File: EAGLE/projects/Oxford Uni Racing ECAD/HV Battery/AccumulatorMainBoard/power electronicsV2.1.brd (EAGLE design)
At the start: 160 x 100 mm, 100 parts, among them IC1 4043D, IC10 74AHC1G08DBV, IC2 SE555D, IC3 4011D, IC5 4043D, IC6 4011D, IC7 4011D, IC8 4011D, IC9 4011D, K1 T9AS1D12-48=T9A, K2 T9AS5D12-12=T9A, K3 T9AS1D12-48=T9A, K4 T9AS1D12-48=T9A, Q1 BSS138, Q2 BSS138, Q3 BSS138, Q4 BSS138

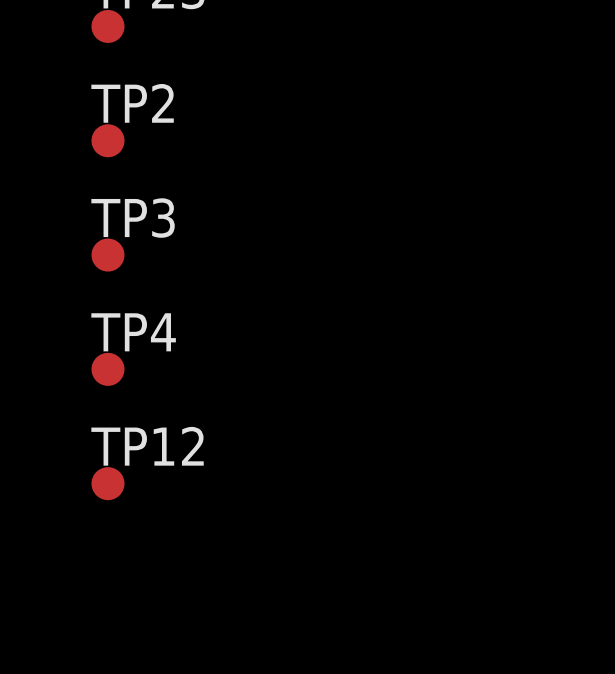
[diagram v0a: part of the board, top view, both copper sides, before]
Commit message: small changes to schematic on acc main board and more feedback
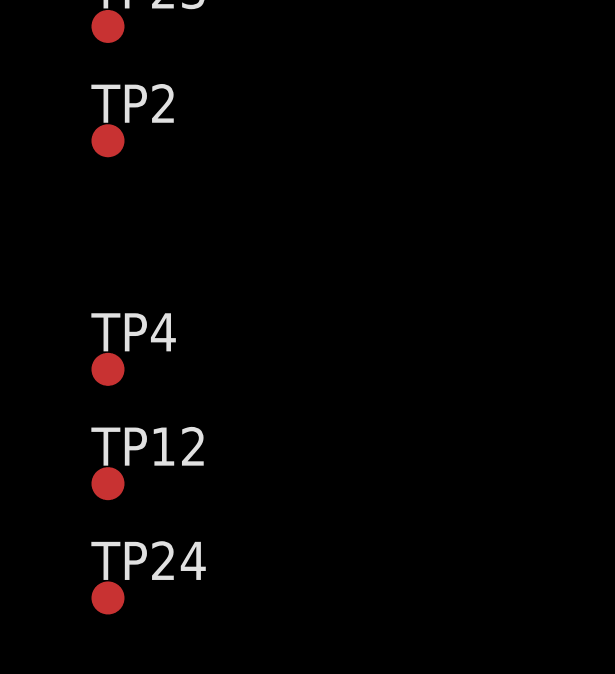
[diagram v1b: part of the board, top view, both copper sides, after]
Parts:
- removed TP3: TPSTP11R, testpad:TP11R
- added TP24: TPSTP11R, testpad:TP11R
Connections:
- net +12V: no longer C9.2, IC1.11, IC1.12, IC1.14, IC1.15, K1.3, K4.4, OK2.5, PRECHARGE/AIRS.3, PRECHARGE/AIRS.4, PRECHARGE/AIRS.6, Q1.2, Q2.2, Q4.2, R13.1, R19.1, R3.2, TP11.TP, TP14.TP, TP3.TP
- net GND: now also C9.2, IC1.11, IC1.12, IC1.14, IC1.15, K1.3, K4.4, OK2.5, PRECHARGE/AIRS.3, PRECHARGE/AIRS.4, PRECHARGE/AIRS.6, Q1.2, Q2.2, Q4.2, R13.1, R19.1, R3.2, TP11.TP, TP14.TP, TP24.TP

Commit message: most of the feedback addressed
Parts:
- removed IC10: 74AHC1G08DBV, 74xx-little-us:SOT23-5
- added LED7, LED8: (no value), led:SML0805
- added R12, R14, R15: (no value), rcl:R0805
- TP1, TP10, TP11, TP12, TP13, TP14, TP15, TP16, TP17, TP18, TP19, TP2, TP20, TP21, TP22, TP23, TP24, TP4, TP5, TP6, TP7: value TPSTP11R -> TPPAD1-17; device testpad:TP11R -> testpad:P1-17
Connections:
- removed net VCC: IC10.5
- new net N$18: LED7.A, R14.1
- new net N$20: LED8.A, R15.1
- new net N$6: IC9.11, IC9.8, IC9.9
- net +12V: now also R14.2, R15.2; no longer IC10.3
- net CHARGE_SAFE: now also IC9.12; no longer IC10.1
- net DISCHARGE_ENABLE: now also R12.2
- net GND: now also R12.1; no longer IC9.12, IC9.13, IC9.8, IC9.9
- net IMD_COIL_OUT: now also LED8.C
- net N$1: now also IC9.10; no longer IC10.4
- net N$13: now also IC9.13; no longer IC10.2
- net N$15: now also LED7.C

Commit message: most of the feedback addressed ctd
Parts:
- removed R17: (no value), rcl:R0805
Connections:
- removed net N$13: IC9.13, LED4.C
- net DISCHARGE_ENABLE: now also IC9.13, LED4.C
- net GND: no longer R17.1
- net N$8: no longer R17.2
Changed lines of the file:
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@@
 <attribute name="VALUE" x="-36.195" y="143.51" size="1.27" layer="27"/>
-</element>
-<element name="R17" library="rcl" library_urn="urn:adsk.eagle:library:334" package="R0805" package3d_urn="urn:adsk.eagle:package:23553/2" value="" x="-41.91" y="146.05" smashed="yes">
-<attribute name="NAME" x="-42.545" y="147.32" size="1.27" layer="25"/>
-<attribute name="POPULARITY" value="86" x="0" y="0" size="1.778" layer="27" display="off"/>
-<attribute name="SPICEPREFIX" value="R" x="0" y="0" size="1.778" layer="27" display="off"/>
-<attribute name="VALUE" x="-42.545" y="143.51" size="1.27" layer="27"/>
 </element>
 <element name="R19" library="rcl" library_urn="urn:adsk.eagle:library:334" package="R0805" package3d_urn="urn:adsk.eagle:package:23553/2" value="" x="-48.26" y="146.05" smashed="yes">
@@
 <contactref element="C1" pad="2"/>
 <contactref element="C2" pad="2"/>
-<contactref element="R17" pad="1"/>
 <contactref element="IC4" pad="3"/>
 <contactref element="C4" pad="2"/>
@@
 <wire x1="-55.56" y1="146.05" x2="-58.74" y2="140.97" width="0" layer="19" extent="1-1"/>
 <wire x1="-49.21" y1="146.05" x2="-55.56" y2="146.05" width="0" layer="19" extent="1-1"/>
-<wire x1="-42.86" y1="146.05" x2="-49.21" y2="146.05" width="0" layer="19" extent="1-1"/>
-<wire x1="-44.72" y1="151.13" x2="-42.86" y2="146.05" width="0" layer="19" extent="1-1"/>
-<wire x1="-36.51" y1="146.05" x2="-42.86" y2="146.05" width="0" layer="19" extent="1-1"/>
+<wire x1="-44.72" y1="151.13" x2="-49.21" y2="146.05" width="0" layer="19" extent="1-1"/>
+<wire x1="-36.51" y1="146.05" x2="-44.72" y2="151.13" width="0" layer="19" extent="1-1"/>
 <wire x1="-28.89" y1="140.97" x2="-36.51" y2="146.05" width="0" layer="19" extent="1-1"/>
 <wire x1="-15.56" y1="140.97" x2="-28.89" y2="140.97" width="0" layer="19" extent="1-1"/>
@@
 <contactref element="TP18" pad="TP"/>
 <contactref element="R12" pad="2"/>
+<contactref element="LED4" pad="C"/>
+<contactref element="IC9" pad="13"/>
 <wire x1="-124.78" y1="-133.35" x2="-125.73" y2="-82.55" width="0" layer="19" extent="1-1"/>
 <wire x1="-118.11" y1="-16.51" x2="-125.73" y2="-82.55" width="0" layer="19" extent="1-1"/>
-<wire x1="-67.31" y1="113.7666" x2="-118.11" y2="-16.51" width="0" layer="19" extent="1-1"/>
+<wire x1="-116.84" y1="119.9134" x2="-118.11" y2="-16.51" width="0" layer="19" extent="1-1"/>
+<wire x1="-92.39" y1="124.53" x2="-116.84" y2="119.9134" width="0" layer="19" extent="1-1"/>
+<wire x1="-92.49" y1="146.05" x2="-92.39" y2="124.53" width="0" layer="19" extent="1-1"/>
+<wire x1="-67.31" y1="113.7666" x2="-92.39" y2="124.53" width="0" layer="19" extent="1-1"/>
 <wire x1="-66.04" y1="113.7666" x2="-67.31" y2="113.7666" width="0" layer="19" extent="1-1"/>
-<wire x1="-92.39" y1="124.53" x2="-67.31" y2="113.7666" width="0" layer="19" extent="1-1"/>
 <wire x1="-38.735" y1="119.9134" x2="-66.04" y2="113.7666" width="0" layer="19" extent="1-1"/>
 <wire x1="-31.75" y1="151.13" x2="-38.735" y2="119.9134" width="0" layer="19" extent="1-1"/>
@@
 </signal>
 <signal name="CHARGE_SAFE">
-<contactref element="LED5" pad="C"/>
 <contactref element="BMS_I/O" pad="2"/>
 <contactref element="IC9" pad="12"/>
+<contactref element="LED5" pad="C"/>
 <wire x1="-115.57" y1="119.9134" x2="-120.65" y2="-16.51" width="0" layer="19" extent="1-1"/>
 <wire x1="-98.84" y1="146.05" x2="-115.57" y2="119.9134" width="0" layer="19" extent="1-1"/>
@@
 <wire x1="-46.72" y1="151.13" x2="-41.275" y2="113.7666" width="0" layer="19" extent="1-1"/>
 <wire x1="-65.09" y1="146.05" x2="-46.72" y2="151.13" width="0" layer="19" extent="1-1"/>
-</signal>
-<signal name="N$13">
-<contactref element="LED4" pad="C"/>
-<contactref element="IC9" pad="13"/>
-<wire x1="-116.84" y1="119.9134" x2="-92.49" y2="146.05" width="0" layer="19" extent="1-1"/>
 </signal>
 <signal name="N$9">
@@
 <contactref element="Q2" pad="1"/>
 <contactref element="TP6" pad="TP"/>
-<contactref element="R17" pad="2"/>
 <contactref element="R24" pad="2"/>
 <contactref element="TP17" pad="TP"/>
@@
 <wire x1="-100.01" y1="124.53" x2="-80.01" y2="119.9134" width="0" layer="19" extent="1-1"/>
 <wire x1="-53.66" y1="146.05" x2="-80.01" y2="119.9134" width="0" layer="19" extent="1-1"/>
-<wire x1="-40.96" y1="146.05" x2="-53.66" y2="146.05" width="0" layer="19" extent="1-1"/>
-<wire x1="-26.67" y1="151.13" x2="-40.96" y2="146.05" width="0" layer="19" extent="1-1"/>
+<wire x1="-26.67" y1="151.13" x2="-53.66" y2="146.05" width="0" layer="19" extent="1-1"/>
 </signal>
 <signal name="N$14">

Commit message: Minor changes to layout added values to RC circuit
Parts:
- C9: value (none) -> DNP
- R2: value (none) -> 0R
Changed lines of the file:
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@@
 <attribute name="VALUE" x="-17.78" y="138.43" size="1.27" layer="27"/>
 </element>
-<element name="C9" library="rcl" library_urn="urn:adsk.eagle:library:334" package="C0805K" package3d_urn="urn:adsk.eagle:package:23681/2" value="" x="-45.72" y="151.13" smashed="yes">
+<element name="C9" library="rcl" library_urn="urn:adsk.eagle:library:334" package="C0805K" package3d_urn="urn:adsk.eagle:package:23681/2" value="DNP" x="-45.72" y="151.13" smashed="yes">
 <attribute name="NAME" x="-46.72" y="152.005" size="1.016" layer="25"/>
 <attribute name="POPULARITY" value="52" x="0" y="0" size="1.778" layer="27" display="off"/>
@@
 <attribute name="VALUE" x="-48.895" y="143.51" size="1.27" layer="27"/>
 </element>
-<element name="R2" library="rcl" library_urn="urn:adsk.eagle:library:334" package="R0805" package3d_urn="urn:adsk.eagle:package:23553/2" value="" x="-66.04" y="146.05" smashed="yes">
+<element name="R2" library="rcl" library_urn="urn:adsk.eagle:library:334" package="R0805" package3d_urn="urn:adsk.eagle:package:23553/2" value="0R" x="-66.04" y="146.05" smashed="yes">
 <attribute name="NAME" x="-66.675" y="147.32" size="1.27" layer="25"/>
 <attribute name="POPULARITY" value="86" x="0" y="0" size="1.778" layer="27" display="off"/>
@@
 <contactref element="IC1" pad="14"/>
 <contactref element="IC1" pad="15"/>
-<contactref element="Q1" pad="2"/>
 <contactref element="R3" pad="2"/>
 <contactref element="OK2" pad="5"/>
@@
 <contactref element="TP14" pad="TP"/>
 <contactref element="TP24" pad="TP"/>
+<contactref element="Q1" pad="2"/>
 <contactref element="R12" pad="1"/>
 <wire x1="-126.68" y1="-133.35" x2="-125.73" y2="-128.27" width="0" layer="19" extent="1-1"/>
@@
 </signal>
 <signal name="DISCHARGE_ENABLE">
-<contactref element="IC3" pad="5"/>
-<contactref element="IC3" pad="6"/>
 <contactref element="Q1" pad="1"/>
 <contactref element="TP7" pad="TP"/>
@@
 <contactref element="LED4" pad="C"/>
 <contactref element="IC9" pad="13"/>
+<contactref element="IC3" pad="5"/>
+<contactref element="IC3" pad="6"/>
 <wire x1="-124.78" y1="-133.35" x2="-125.73" y2="-82.55" width="0" layer="19" extent="1-1"/>
 <wire x1="-118.11" y1="-16.51" x2="-125.73" y2="-82.55" width="0" layer="19" extent="1-1"/>

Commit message: Removed some testpoints and added a few. Also fixed EMSDC relay path
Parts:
- removed R13: (no value), rcl:R0805
- removed TP14, TP15, TP18, TP22: TPPAD1-17, testpad:P1-17
- added TP3: TPPAD1-17, testpad:P1-17
- moved TP6 335.0 mm to (-125.7, -168.9)
- moved TP11 106.7 mm to (-125.7, -174.0)
- moved TP2 45.7 mm to (-125.7, -158.8)
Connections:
- new net N$13: EMSDC.1, K4.3
- new net N$21: K1.3, K4.4
- net +12V: no longer EMSDC.1, K4.3, TP15.TP, TP22.TP
- net CHARGE_SAFE: now also TP3.TP
- net DISCHARGE_ENABLE: now also TP6.TP; no longer TP18.TP
- net GND: no longer K1.3, K4.4, R13.1, TP11.TP, TP14.TP
- net N$10: no longer TP2.TP
- net N$16: now also TP2.TP
- net N$6: now also TP11.TP
- net N$8: no longer TP6.TP
- net N$9: no longer R13.2

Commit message: Updates to the accumulator main board
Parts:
- removed TP13, TP19, TP20: TPPAD1-17, testpad:P1-17
- added TP14: TPPAD1-17, testpad:P1-17
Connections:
- net GND: now also Q3.2
- net IMD_COIL_OUT: now also TP14.TP; no longer Q3.2, TP19.TP
- net N$14: no longer TP13.TP
- net N$9: no longer TP20.TP
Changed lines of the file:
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@@
 <attribute name="VALUE" x="-110.09" y="-57.3" size="1.27" layer="27" align="center"/>
-</element>
-<element name="TP19" library="testpad" library_urn="urn:adsk.eagle:library:385" package="P1-17" package3d_urn="urn:adsk.eagle:package:27949/1" value="TPPAD1-17" x="-125.73" y="-71.12" smashed="yes">
-<attribute name="NAME" x="-126.2799" y="-70.5201" size="1.27" layer="25"/>
-<attribute name="POPULARITY" value="0" x="-125.73" y="-71.12" size="1.778" layer="27" display="off"/>
-<attribute name="TP_SIGNAL_NAME" value="" x="-125.73" y="-73.025" size="1" layer="37"/>
-<attribute name="VALUE" x="-126.238" y="-71.628" size="0.0254" layer="27"/>
 </element>
 <element name="TP17" library="testpad" library_urn="urn:adsk.eagle:library:385" package="P1-17" package3d_urn="urn:adsk.eagle:package:27949/1" value="TPPAD1-17" x="-125.73" y="-74.93" smashed="yes">
@@
 <attribute name="VALUE" x="-126.238" y="-75.438" size="0.0254" layer="27"/>
 </element>
-<element name="TP20" library="testpad" library_urn="urn:adsk.eagle:library:385" package="P1-17" package3d_urn="urn:adsk.eagle:package:27949/1" value="TPPAD1-17" x="-125.73" y="-78.74" smashed="yes">
-<attribute name="NAME" x="-126.2799" y="-78.1401" size="1.27" layer="25"/>
-<attribute name="POPULARITY" value="0" x="-125.73" y="-78.74" size="1.778" layer="27" display="off"/>
-<attribute name="TP_SIGNAL_NAME" value="" x="-125.73" y="-80.645" size="1" layer="37"/>
-<attribute name="VALUE" x="-126.238" y="-79.248" size="0.0254" layer="27"/>
-</element>
 <element name="TP16" library="testpad" library_urn="urn:adsk.eagle:library:385" package="P1-17" package3d_urn="urn:adsk.eagle:package:27949/1" value="TPPAD1-17" x="-125.73" y="-86.36" smashed="yes">
 <attribute name="NAME" x="-126.2799" y="-85.7601" size="1.27" layer="25"/>
@@
 <attribute name="VALUE" x="-126.238" y="-90.678" size="0.0254" layer="27"/>
 </element>
-<element name="TP13" library="testpad" library_urn="urn:adsk.eagle:library:385" package="P1-17" package3d_urn="urn:adsk.eagle:package:27949/1" value="TPPAD1-17" x="-125.73" y="-101.6" smashed="yes">
-<attribute name="NAME" x="-126.2799" y="-101.0001" size="1.27" layer="25"/>
-<attribute name="POPULARITY" value="0" x="-125.73" y="-101.6" size="1.778" layer="27" display="off"/>
-<attribute name="TP_SIGNAL_NAME" value="" x="-125.73" y="-103.505" size="1" layer="37"/>
-<attribute name="VALUE" x="-126.238" y="-102.108" size="0.0254" layer="27"/>
-</element>
 <element name="TP23" library="testpad" library_urn="urn:adsk.eagle:library:385" package="P1-17" package3d_urn="urn:adsk.eagle:package:27949/1" value="TPPAD1-17" x="-125.73" y="-109.22" smashed="yes">
 <attribute name="NAME" x="-126.2799" y="-108.6201" size="1.27" layer="25"/>
@@
 <attribute name="TP_SIGNAL_NAME" value="" x="-125.73" y="-173.99" size="1.778" layer="27" display="off"/>
 <attribute name="VALUE" x="-125.73" y="-173.99" size="0.0254" layer="27"/>
+</element>
+<element name="TP14" library="testpad" library_urn="urn:adsk.eagle:library:385" package="P1-17" package3d_urn="urn:adsk.eagle:package:27949/1" value="TPPAD1-17" x="-125.73" y="-179.07" smashed="yes">
+<attribute name="NAME" x="-126.873" y="-177.673" size="1.27" layer="25" ratio="10"/>
+<attribute name="POPULARITY" value="0" x="-125.73" y="-179.07" size="1.778" layer="27" display="off"/>
+<attribute name="TP_SIGNAL_NAME" value="" x="-127" y="-182.245" size="1" layer="37"/>
+<attribute name="VALUE" x="-125.73" y="-179.07" size="0.0254" layer="27"/>
 </element>
 </elements>
@@
 <contactref element="IC1" pad="12"/>
 <contactref element="C9" pad="2"/>
-<contactref element="Q2" pad="2"/>
 <contactref element="TP24" pad="TP"/>
 <contactref element="Q1" pad="2"/>
 <contactref element="R12" pad="1"/>
+<contactref element="Q3" pad="2"/>
+<contactref element="Q2" pad="2"/>
 <wire x1="-126.68" y1="-133.35" x2="-125.73" y2="-128.27" width="0" layer="19" extent="1-1"/>
 <wire x1="-120.65" y1="-7.62" x2="-125.73" y2="-128.27" width="0" layer="19" extent="1-1"/>
@@
 <wire x1="-98.11" y1="124.53" x2="-99.06" y2="113.7666" width="0" layer="19" extent="1-1"/>
 <wire x1="-90.49" y1="124.53" x2="-98.11" y2="124.53" width="0" layer="19" extent="1-1"/>
-<wire x1="-99.38" y1="133.35" x2="-98.11" y2="124.53" width="0" layer="19" extent="1-1"/>
-<wire x1="-105.28" y1="133.35" x2="-99.38" y2="133.35" width="0" layer="19" extent="1-1"/>
+<wire x1="-105.73" y1="124.53" x2="-98.11" y2="124.53" width="0" layer="19" extent="1-1"/>
+<wire x1="-113.35" y1="124.53" x2="-105.73" y2="124.53" width="0" layer="19" extent="1-1"/>
+<wire x1="-105.28" y1="133.35" x2="-105.73" y2="124.53" width="0" layer="19" extent="1-1"/>
+<wire x1="-99.38" y1="133.35" x2="-105.28" y2="133.35" width="0" layer="19" extent="1-1"/>
 <wire x1="-93.03" y1="133.35" x2="-99.38" y2="133.35" width="0" layer="19" extent="1-1"/>
 <wire x1="-86.68" y1="133.35" x2="-93.03" y2="133.35" width="0" layer="19" extent="1-1"/>
@@
 <wire x1="-69.53" y1="133.35" x2="-73.98" y2="133.35" width="0" layer="19" extent="1-1"/>
 <wire x1="-112.08" y1="133.35" x2="-105.28" y2="133.35" width="0" layer="19" extent="1-1"/>
-<wire x1="-113.35" y1="124.53" x2="-112.08" y2="133.35" width="0" layer="19" extent="1-1"/>
 <wire x1="-87.63" y1="113.7666" x2="-90.49" y2="124.53" width="0" layer="19" extent="1-1"/>
 <wire x1="-87.63" y1="107.95" x2="-87.63" y2="113.7666" width="0" layer="19" extent="1-1"/>
@@
 <contactref element="K1" pad="2"/>
 <contactref element="D8" pad="A"/>
-<contactref element="Q3" pad="2"/>
-<contactref element="TP19" pad="TP"/>
 <contactref element="LED8" pad="C"/>
-<wire x1="-125.51" y1="-153.67" x2="-125.73" y2="-71.12" width="0" layer="19" extent="1-1"/>
-<wire x1="-34.29" y1="8.89" x2="-125.73" y2="-71.12" width="0" layer="19" extent="1-1"/>
-<wire x1="-72.73" y1="125.73" x2="-34.29" y2="8.89" width="0" layer="19" extent="1-1"/>
+<contactref element="TP14" pad="TP"/>
 <wire x1="-99.06" y1="126.93" x2="-72.73" y2="125.73" width="0" layer="19" extent="1-1"/>
-<wire x1="-105.73" y1="124.53" x2="-99.06" y2="126.93" width="0" layer="19" extent="1-1"/>
+<wire x1="-34.29" y1="8.89" x2="-72.73" y2="125.73" width="0" layer="19" extent="1-1"/>
+<wire x1="-125.51" y1="-153.67" x2="-34.29" y2="8.89" width="0" layer="19" extent="1-1"/>
+<wire x1="-125.73" y1="-179.07" x2="-125.51" y2="-153.67" width="0" layer="19" extent="1-1"/>
 </signal>
 <signal name="CHARGE_SAFE">
@@
 <contactref element="TP5" pad="TP"/>
 <contactref element="R25" pad="2"/>
-<contactref element="TP20" pad="TP"/>
-<wire x1="-107.63" y1="124.53" x2="-125.73" y2="-78.74" width="0" layer="19" extent="1-1"/>
-<wire x1="-60.01" y1="146.05" x2="-107.63" y2="124.53" width="0" layer="19" extent="1-1"/>
+<wire x1="-60.01" y1="146.05" x2="-21.59" y2="151.13" width="0" layer="19" extent="1-1"/>
 <wire x1="-46.355" y1="113.7666" x2="-60.01" y2="146.05" width="0" layer="19" extent="1-1"/>
-<wire x1="-21.59" y1="151.13" x2="-60.01" y2="146.05" width="0" layer="19" extent="1-1"/>
+<wire x1="-107.63" y1="124.53" x2="-60.01" y2="146.05" width="0" layer="19" extent="1-1"/>
 </signal>
 <signal name="N$8">
@@
 <contactref element="K1" pad="4"/>
 <contactref element="EMSDC" pad="2"/>
-<contactref element="TP13" pad="TP"/>
-<wire x1="-20.32" y1="24.13" x2="-125.73" y2="-101.6" width="0" layer="19" extent="1-1"/>
 <wire x1="-91.03" y1="91.44" x2="-20.32" y2="24.13" width="0" layer="19" extent="1-1"/>
 </signal>
